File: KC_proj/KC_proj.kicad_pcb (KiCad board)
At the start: 4 copper layers, 42.2 x 46.4 mm, 30 parts, among them J1 Conn_01x05_Socket, J3 USB_C_Receptacle_USB2.0_14P, SW1 SW_Push, SW2 SW_Push, U1 STM32C071KBTx, U2 AMS1117-3.3, U4 TPS2116DRL

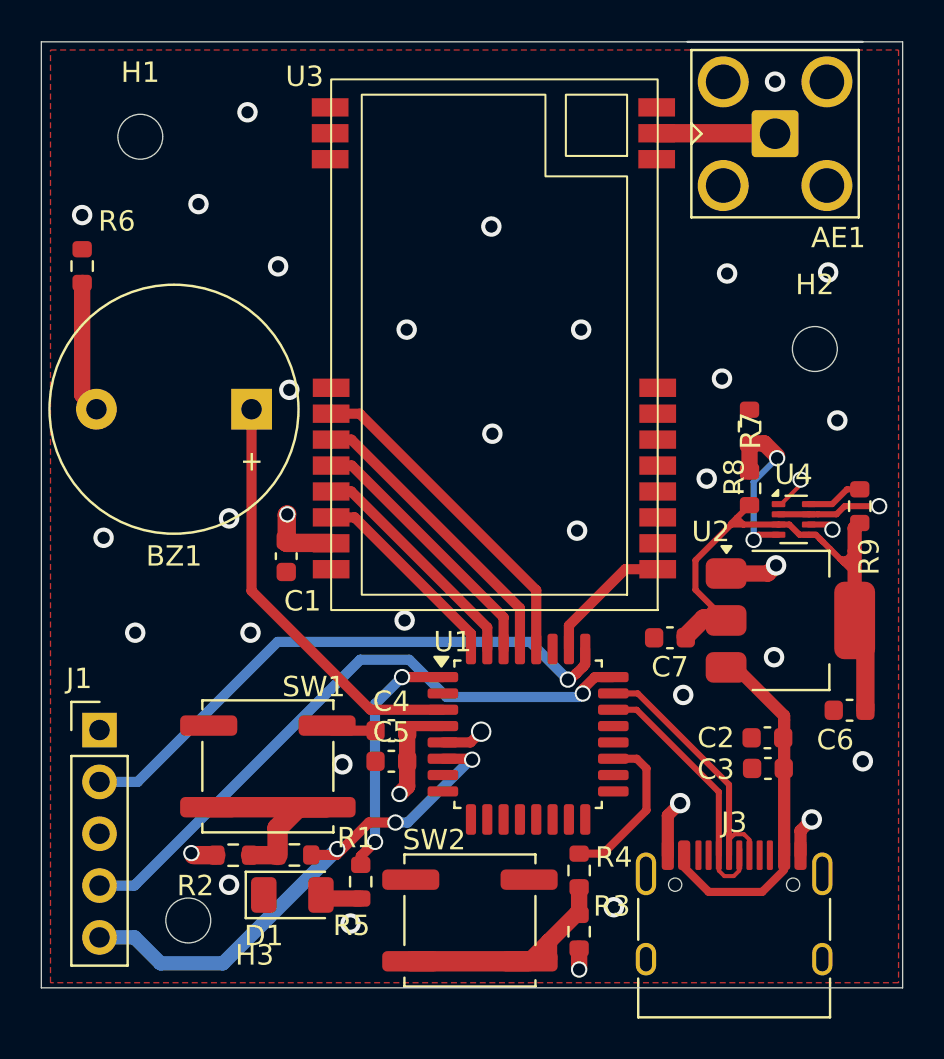
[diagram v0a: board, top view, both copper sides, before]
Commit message: Update libs and kicad
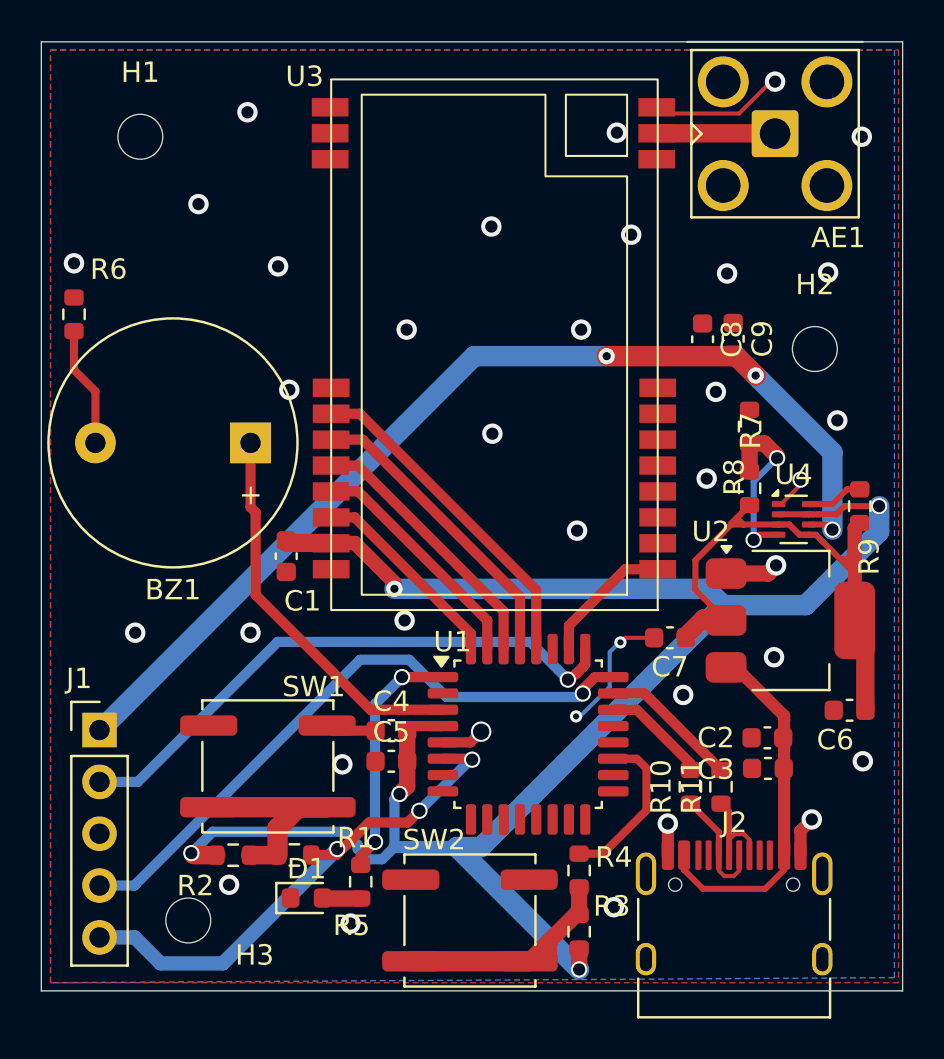
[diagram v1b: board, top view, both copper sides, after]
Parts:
- removed J3: USB_C_Receptacle_USB2.0_14P, Connector_USB:USB_C_Receptacle_HRO_TYPE-C-31-M-12
- added C8: 100n, Capacitor_SMD:C_0603_1608Metric, F.Cu at (151.7, 72.9)
- added C9: 22u, Capacitor_SMD:C_0603_1608Metric, F.Cu at (153.2, 72.9)
- added J2: USB_C_Receptacle_USB2.0_14P, Connector_USB:USB_C_Receptacle_HRO_TYPE-C-31-M-12, F.Cu at (153.2, 102.2)
- added R10: 5.1k, Resistor_SMD:R_0603_1608Metric, F.Cu at (151.1, 94.8)
- added R11: 5.1k, Resistor_SMD:R_0603_1608Metric, F.Cu at (152.6, 94.8)
- D1: footprint LED_SMD:LED_1206_3216Metric -> LED_SMD:LED_0603_1608Metric
- R5: value 250 -> 200
- R6: value 165 -> 200
- moved R6 2.40 mm to (120.9, 71.7)
- moved BZ1 1.65 mm to (129.6, 78.0)
- moved D1 0.72 mm to (132.3, 100.3)
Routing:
- net +3V3: track 16.1 -> 89.2 mm
- net GND: track 14.4 -> 26.6 mm, vias 33 -> 36
- net /USB_D-: track 13.5 -> 5.18 mm
- net /STLink_3v3: track 42.4 -> 50.6 mm, vias 1 -> 3
- net /USB_D+: track 14.6 -> 6.83 mm
- net Net-(J2-D--PadA7): track 0.00 -> 5.84 mm
- net Net-(J2-D+-PadA6): track 0.00 -> 5.43 mm
- net /BZR: track 20.7 -> 19.1 mm
- net Net-(BZ1--): track 6.46 -> 5.91 mm
- added copper zone on B.Cu, net GND
- removed copper zone on In2.Cu, net +3V3
- removed copper zone on In1.Cu, net GND
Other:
- board size 42.2 x 46.4 mm -> 42.2 x 46.5 mm
- copper layers 4 -> 2
- board text added: "Liquid Rocketry at Illinois HAL-1-GND MKI"
